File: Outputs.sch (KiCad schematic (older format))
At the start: 21 parts

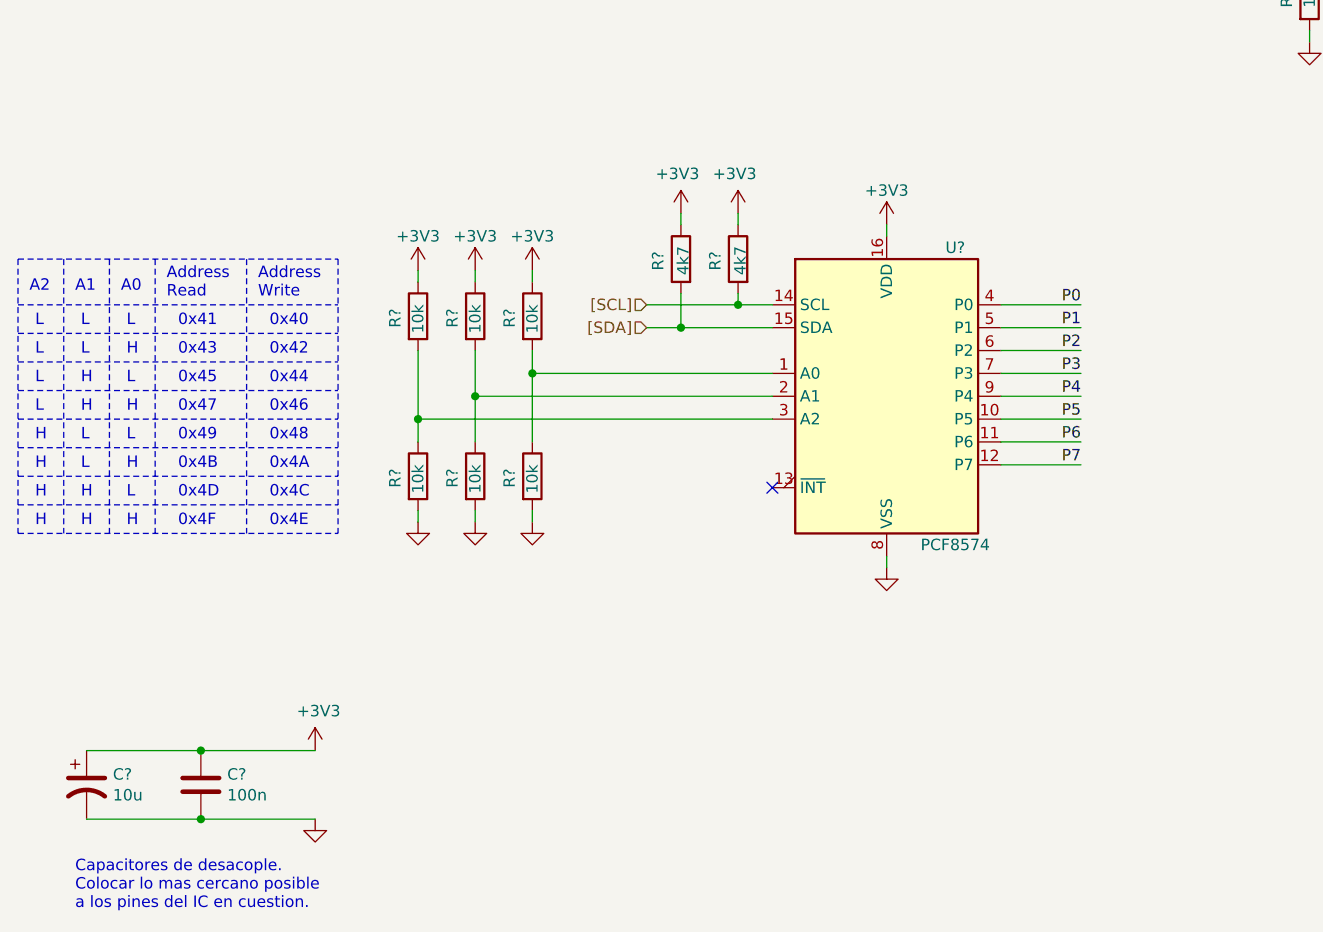
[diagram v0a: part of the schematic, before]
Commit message: Arreglos.
    * Arreglo referencias de address de salida(PCF8574)
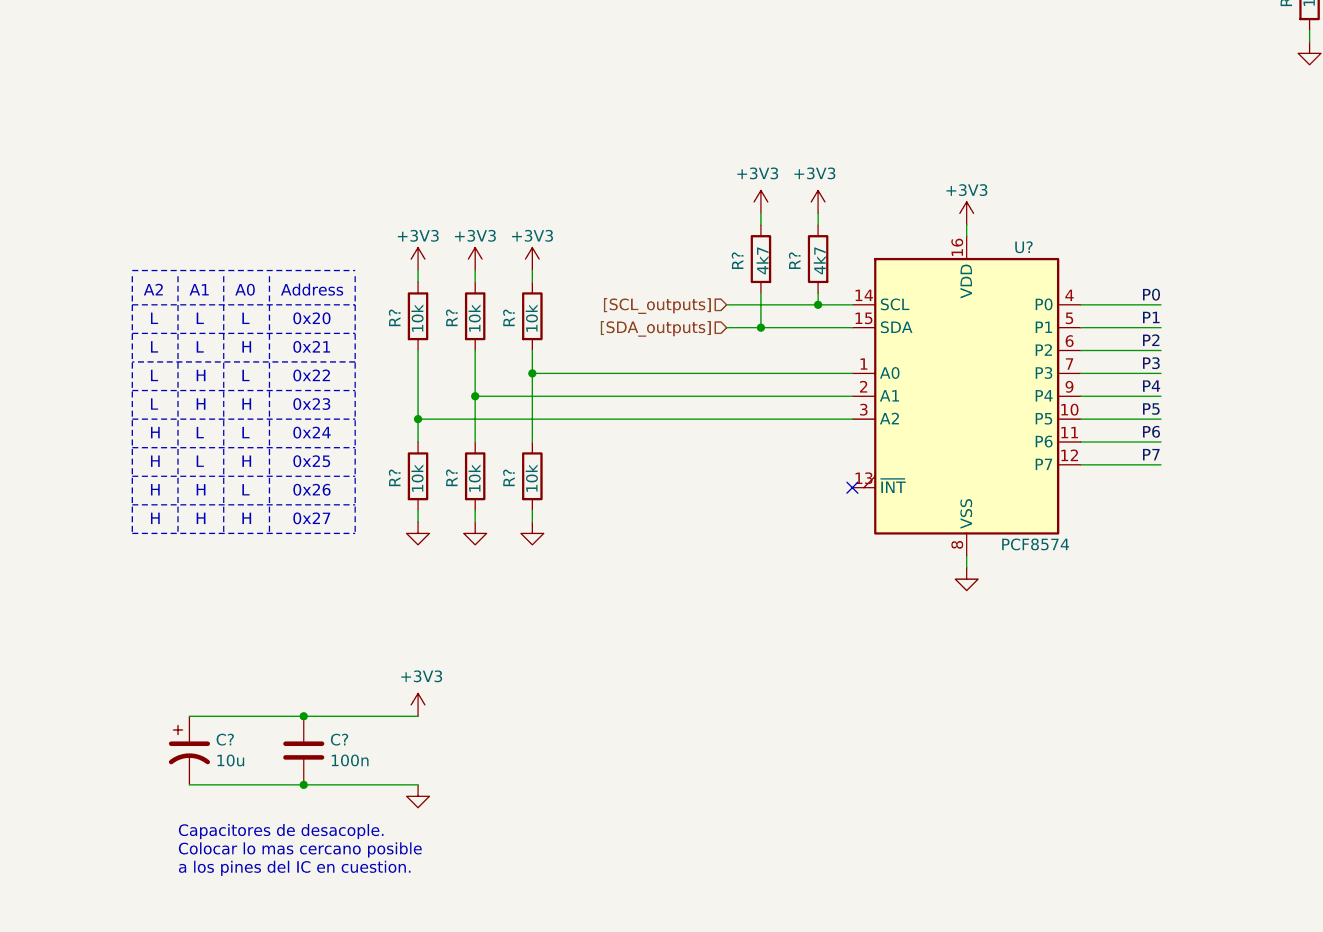
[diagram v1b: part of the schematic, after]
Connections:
- net [SCL] renamed [SCL_outputs]
- net [SDA] renamed [SDA_outputs]
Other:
- note added: "0x20"
- note added: "0x21"
- note added: "0x22"
- note added: "0x23"
- note added: "0x24"
- note added: "0x25"
- note added: "0x26"
- note added: "0x27"
- note added: "Address"
- note removed: "0x40"
- note removed: "0x41"
- note removed: "0x42"
- note removed: "0x43"
- note removed: "0x44"
- note removed: "0x45"
- note removed: "0x46"
- note removed: "0x47"
- note removed: "0x48"
- note removed: "0x49"
- note removed: "0x4A"
- note removed: "0x4B"
- note removed: "0x4C"
- note removed: "0x4D"
- note removed: "0x4E"
- note removed: "0x4F"
- note removed: "Address\nRead"
- note removed: "Address\nWrite"
- moved on the sheet: C?, R?, U?
